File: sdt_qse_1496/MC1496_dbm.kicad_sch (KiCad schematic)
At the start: 26 parts

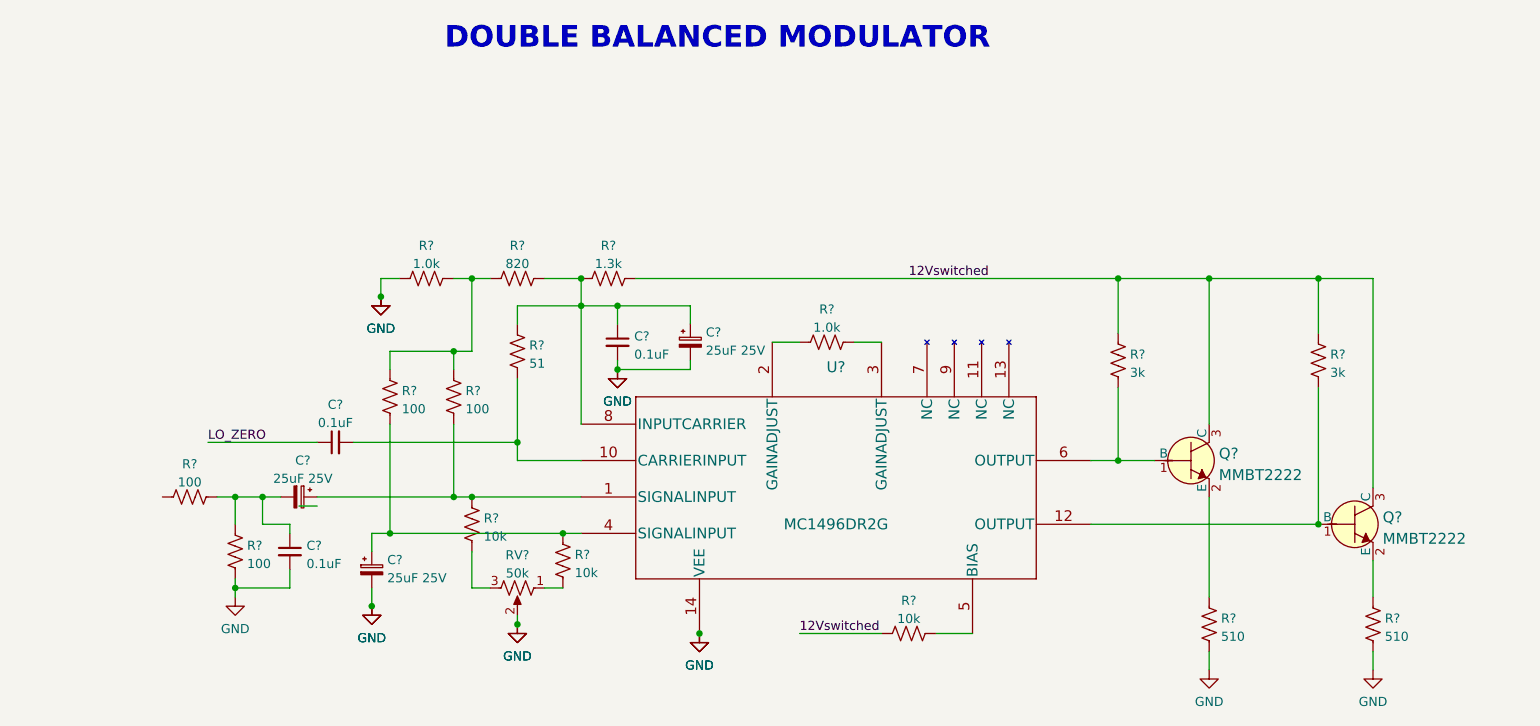
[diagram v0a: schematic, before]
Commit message: Some improvements to the MC1496 simulations.
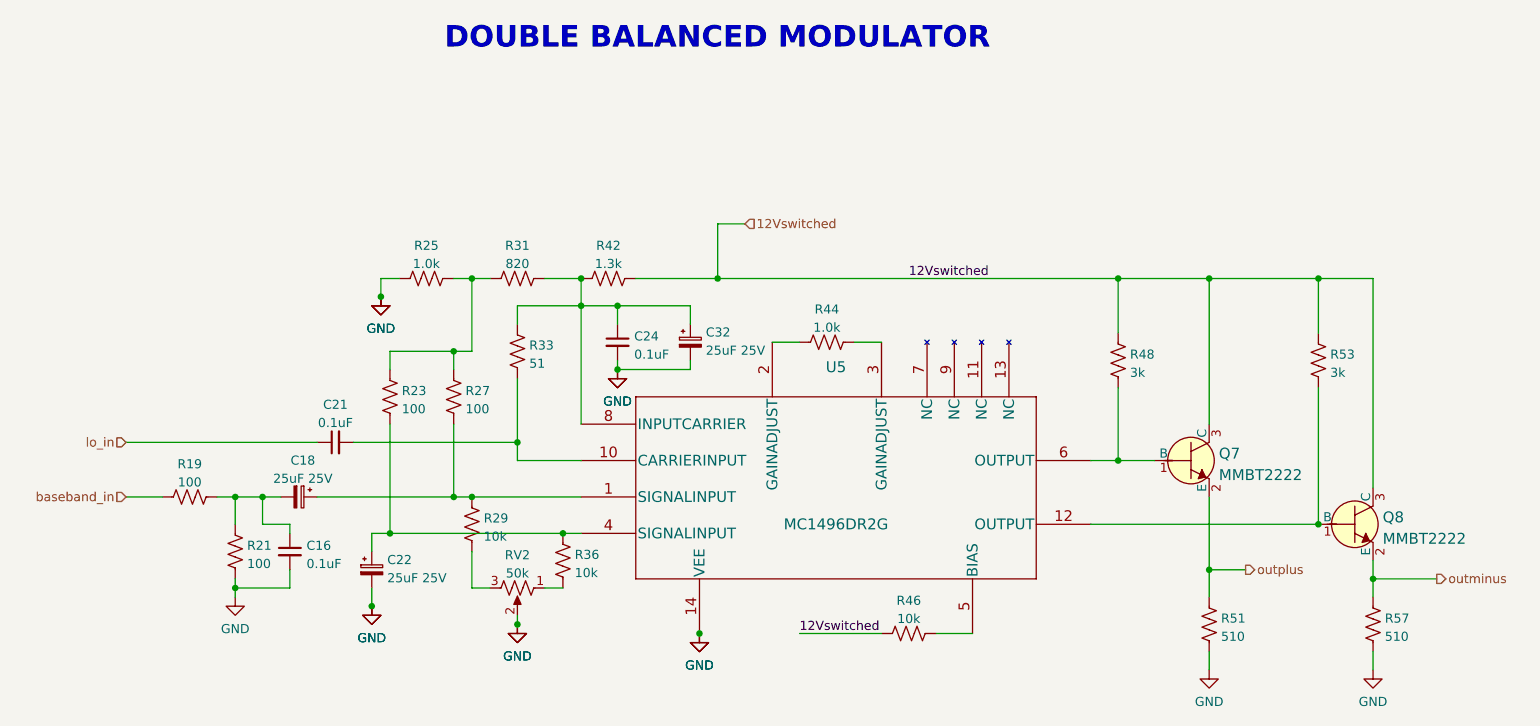
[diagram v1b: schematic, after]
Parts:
- gave numbers to parts that had none: 26
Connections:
- net outminus: now reaches Q8.2 (E), R57.1
- net outplus: now reaches Q7.2 (E), R51.1
- net baseband_in: now reaches R19.1
- net LO_ZERO renamed lo_in

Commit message: Finishing layout of version2.
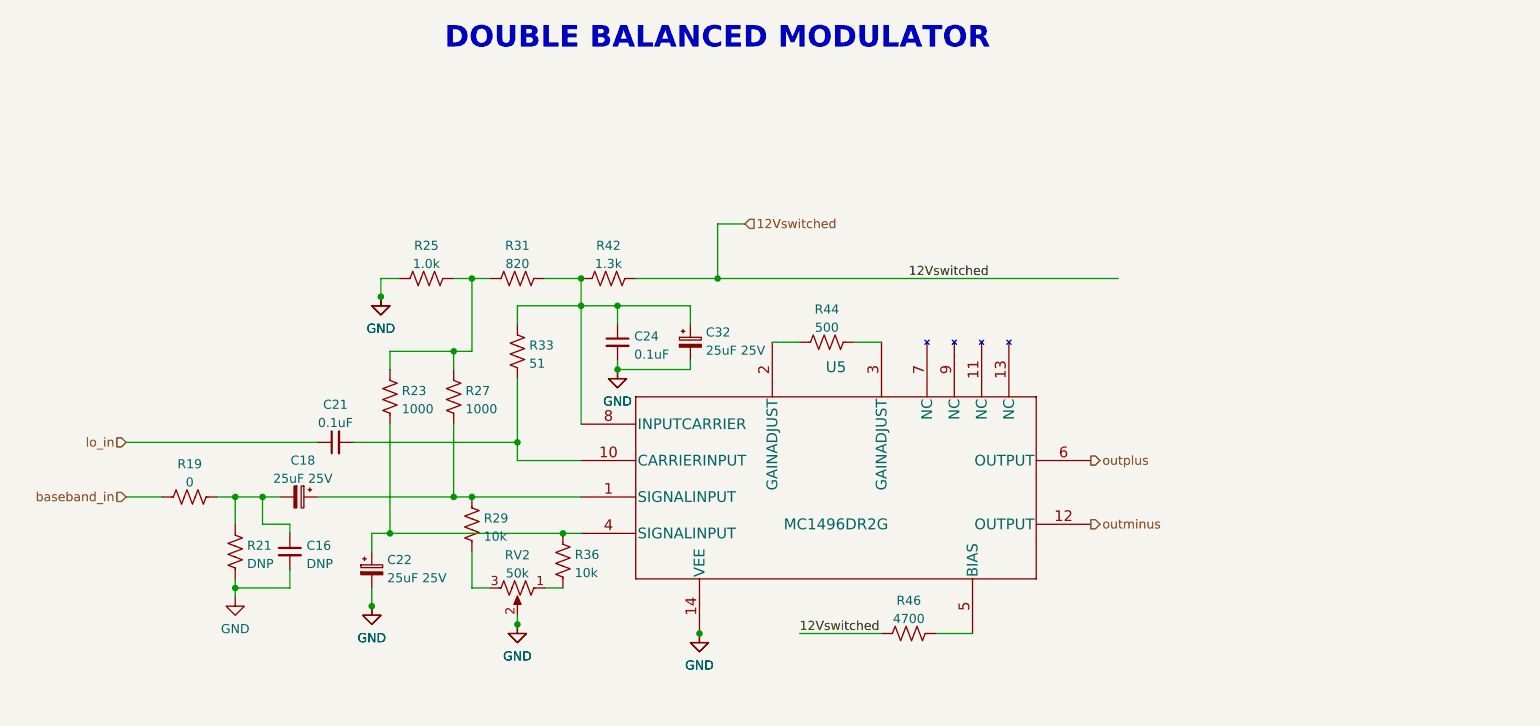
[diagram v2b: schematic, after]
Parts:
- removed Q7, Q8: MMBT2222, digikey-footprints:SOT-23-3, symbol dk_Transistors-Bipolar-BJT-Single:MMBT2222LT1G
- removed R48, R53: 3k, Resistor_SMD:R_1206_3216Metric, symbol Device:R_US
- removed R51, R57: 510, Resistor_SMD:R_1206_3216Metric, symbol Device:R_US
- C16: value 0.1uF -> DNP
- R19: value 100 -> 0
- R21: value 100 -> DNP
- R23, R27: value 100 -> 1000
- R44: value 1.0k -> 500
- R46: value 10k -> 4700
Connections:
- net outminus: now also U5.12 (OUTPUT)
- net outplus: now also U5.6 (OUTPUT)

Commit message: New simulations added.
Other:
- note added: "An audio bypass needed here?"
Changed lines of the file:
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@@
     (effects (font (size 3 3) (thickness 0.6) bold) (justify left bottom))
+  )
+  (text "An audio bypass needed here?" (at 105.41 68.58 90)
+    (effects (font (size 1.27 1.27)) (justify left bottom))
   )
   (label "12Vswitched" (at 151.13 119.38 0)

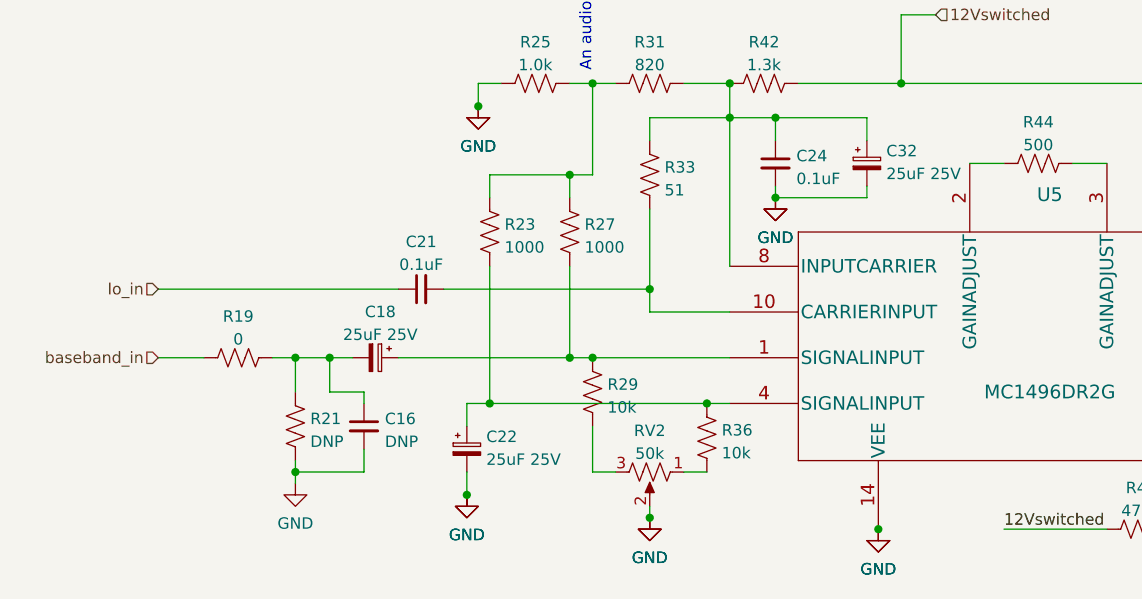
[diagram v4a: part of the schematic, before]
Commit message: Added Sallen Key filters to schematic.
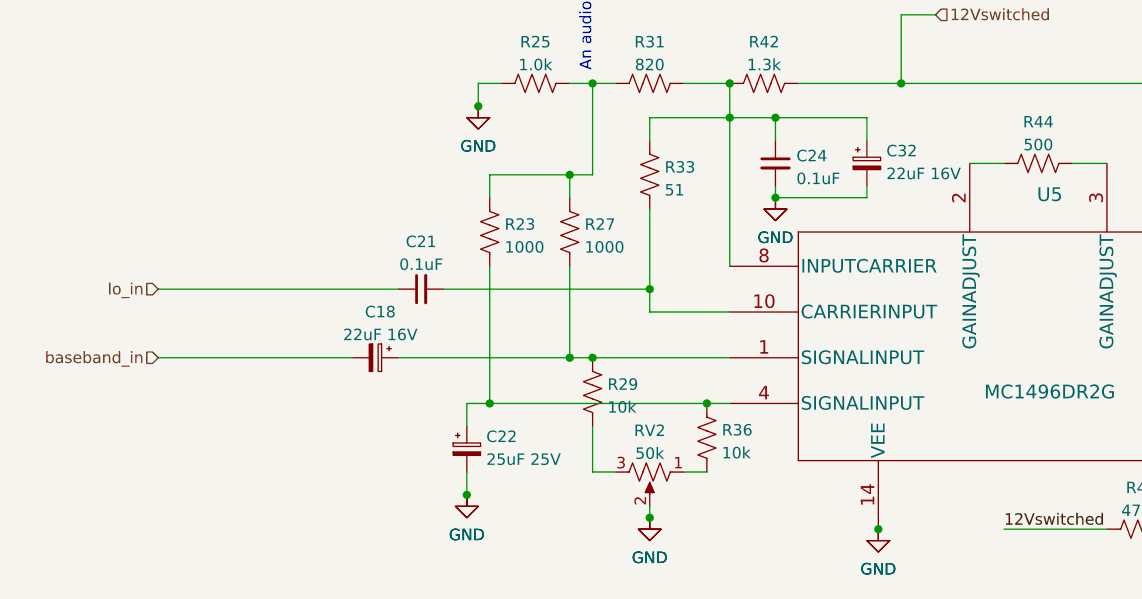
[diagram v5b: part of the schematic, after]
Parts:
- removed C16: DNP, Capacitor_SMD:C_1206_3216Metric, symbol Device:C_Small
- removed R19: 0, Resistor_SMD:R_1206_3216Metric, symbol Device:R_US
- removed R21: DNP, Resistor_SMD:R_1206_3216Metric, symbol Device:R_US
- C18, C32: value 25uF 25V -> 22uF 16V; footprint Capacitor_THT:CP_Radial_D5.0mm_P2.00mm -> Capacitor_SMD:C_1206_3216Metric
- C22: footprint Capacitor_THT:CP_Radial_D5.0mm_P2.00mm -> Capacitor_SMD:C_1206_3216Metric
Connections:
- net baseband_in: now also C18.2

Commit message: Almost ready to release Prototype 3.
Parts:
- C18, C32: value 22uF 16V -> 22uF
- C22: value 25uF 25V -> 22uF
- R31: value 820 -> 1.0k
- R42: value 1.3k -> 1.0k
- R44: value 500 -> 470
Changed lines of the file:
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@@
   (symbol (lib_id "Device:R_US") (at 154.94 78.74 90) (unit 1)
     (in_bom yes) (on_board yes) (dnp no) (fields_autoplaced)
-    (property "Reference" "R44" (at 154.94 74.1512 90)
-      (effects (font (size 1.27 1.27)))
-    )
-    (property "Value" "500" (at 154.94 76.6881 90)
+    (property "Reference" "R44" (at 154.94 73.66 90)
+      (effects (font (size 1.27 1.27)))
+    )
+    (property "Value" "470" (at 154.94 76.2 90)
       (effects (font (size 1.27 1.27)))
     )
@@
       (effects (font (size 1.27 1.27)))
     )
-    (property "Value" "22uF 16V" (at 81.8261 97.79 90)
+    (property "Value" "22uF" (at 81.8261 97.79 90)
       (effects (font (size 1.27 1.27)))
     )
@@
   (symbol (lib_id "Device:C_Polarized_Small") (at 91.44 110.49 0) (unit 1)
     (in_bom yes) (on_board yes) (dnp no) (fields_autoplaced)
-    (property "Reference" "C22" (at 93.599 109.1092 0)
-      (effects (font (size 1.27 1.27)) (justify left))
-    )
-    (property "Value" "25uF 25V" (at 93.599 111.6461 0)
+    (property "Reference" "C22" (at 93.98 109.3089 0)
+      (effects (font (size 1.27 1.27)) (justify left))
+    )
+    (property "Value" "22uF" (at 93.98 111.8489 0)
       (effects (font (size 1.27 1.27)) (justify left))
     )
@@
   (symbol (lib_id "Device:C_Polarized_Small") (at 135.89 78.74 0) (unit 1)
     (in_bom yes) (on_board yes) (dnp no) (fields_autoplaced)
-    (property "Reference" "C32" (at 138.049 77.3592 0)
-      (effects (font (size 1.27 1.27)) (justify left))
-    )
-    (property "Value" "22uF 16V" (at 138.049 79.8961 0)
+    (property "Reference" "C32" (at 138.43 77.5589 0)
+      (effects (font (size 1.27 1.27)) (justify left))
+    )
+    (property "Value" "22uF" (at 138.43 80.0989 0)
       (effects (font (size 1.27 1.27)) (justify left))
     )
@@
   (symbol (lib_id "Device:R_US") (at 111.76 69.85 90) (unit 1)
     (in_bom yes) (on_board yes) (dnp no) (fields_autoplaced)
-    (property "Reference" "R31" (at 111.76 65.2612 90)
-      (effects (font (size 1.27 1.27)))
-    )
-    (property "Value" "820" (at 111.76 67.7981 90)
+    (property "Reference" "R31" (at 111.76 64.77 90)
+      (effects (font (size 1.27 1.27)))
+    )
+    (property "Value" "1.0k" (at 111.76 67.31 90)
       (effects (font (size 1.27 1.27)))
     )
@@
   (symbol (lib_id "Device:R_US") (at 124.46 69.85 90) (unit 1)
     (in_bom yes) (on_board yes) (dnp no) (fields_autoplaced)
-    (property "Reference" "R42" (at 124.46 65.2612 90)
-      (effects (font (size 1.27 1.27)))
-    )
-    (property "Value" "1.3k" (at 124.46 67.7981 90)
-      (effects (font (size 1.27 1.27)))
-    )
+    (property "Reference" "R42" (at 124.46 64.77 90)
+      (effects (font (size 1.27 1.27)))
+    )
+    (property "Value" "1.0k" (at 124.46 67.31 90)
+      (effects (font (size 1.27 1.27)))
+    )

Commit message: Checked gerbers, releasing to PCBWay.
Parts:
- C18, C22, C32: footprint Capacitor_SMD:C_1206_3216Metric -> Capacitor_Tantalum_SMD:CP_EIA-3216-10_Kemet-I
- R23, R27: value 1000 -> 1.0k
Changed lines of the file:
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@@
       (effects (font (size 1.27 1.27)))
     )
-    (property "Footprint" "Capacitor_SMD:C_1206_3216Metric" (at 81.28 100.33 0)
+    (property "Footprint" "Capacitor_Tantalum_SMD:CP_EIA-3216-10_Kemet-I" (at 81.28 100.33 0)
       (effects (font (size 1.27 1.27)) hide)
     )
@@
       (effects (font (size 1.27 1.27)) (justify left))
     )
-    (property "Footprint" "Capacitor_SMD:C_1206_3216Metric" (at 91.44 110.49 0)
+    (property "Footprint" "Capacitor_Tantalum_SMD:CP_EIA-3216-10_Kemet-I" (at 91.44 110.49 0)
       (effects (font (size 1.27 1.27)) hide)
     )
@@
       (effects (font (size 1.27 1.27)) (justify left))
     )
-    (property "Footprint" "Capacitor_SMD:C_1206_3216Metric" (at 135.89 78.74 0)
+    (property "Footprint" "Capacitor_Tantalum_SMD:CP_EIA-3216-10_Kemet-I" (at 135.89 78.74 0)
       (effects (font (size 1.27 1.27)) hide)
     )
@@
   (symbol (lib_id "Device:R_US") (at 102.87 86.36 0) (unit 1)
     (in_bom yes) (on_board yes) (dnp no) (fields_autoplaced)
-    (property "Reference" "R27" (at 104.521 85.5253 0)
-      (effects (font (size 1.27 1.27)) (justify left))
-    )
-    (property "Value" "1000" (at 104.521 88.0622 0)
+    (property "Reference" "R27" (at 105.41 85.725 0)
+      (effects (font (size 1.27 1.27)) (justify left))
+    )
+    (property "Value" "1.0k" (at 105.41 88.265 0)
       (effects (font (size 1.27 1.27)) (justify left))
     )
@@
   (symbol (lib_id "Device:R_US") (at 93.98 86.36 0) (unit 1)
     (in_bom yes) (on_board yes) (dnp no) (fields_autoplaced)
-    (property "Reference" "R23" (at 95.631 85.5253 0)
-      (effects (font (size 1.27 1.27)) (justify left))
-    )
-    (property "Value" "1000" (at 95.631 88.0622 0)
-      (effects (font (size 1.27 1.27)) (justify left))
-    )
+    (property "Reference" "R23" (at 96.52 85.725 0)
+      (effects (font (size 1.27 1.27)) (justify left))
+    )
+    (property "Value" "1.0k" (at 96.52 88.265 0)
+      (effects (font (size 1.27 1.27)) (justify left))
+    )
